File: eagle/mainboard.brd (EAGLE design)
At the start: 100 x 100 mm, 100 parts, among them IC1 74HC02D, IC2 74HC151D, IC3 74HC151D, IC4 74HC590D

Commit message: set board labels and fixed errors
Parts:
- moved C8 1.00 mm to (86.2, -26.8)
- moved R10 0.64 mm to (90.1, 55.0)
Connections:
- net GND: no longer POWER-IN.S1, POWER-IN.S2, POWER-IN.S3, POWER-IN.S4, USB-CONTROLLER1.S1, USB-CONTROLLER1.S2, USB-CONTROLLER1.S3, USB-CONTROLLER1.S4, USB-CONTROLLER2.S1, USB-CONTROLLER2.S2, USB-CONTROLLER2.S3, USB-CONTROLLER2.S4, USB-CONTROLLER3.S1, USB-CONTROLLER3.S2, USB-CONTROLLER3.S3, USB-CONTROLLER3.S4, USB-CONTROLLER4.S1, USB-CONTROLLER4.S2, USB-CONTROLLER4.S3, USB-CONTROLLER4.S4
- net GNDA: no longer CONTROLLER-IN.S1, CONTROLLER-IN.S2, CONTROLLER-IN.S3, CONTROLLER-IN.S4
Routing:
- net VCC: track 15.6 -> 33.7 mm, vias 3 -> 6
- net GND: track 6.55 -> 21.2 mm, vias 3 -> 10
- net N$32: track 3.69 -> 12.6 mm, vias 1 -> 2
- net N$29: track 29.6 -> 36.7 mm
- net GNDA: track 16.7 -> 20.7 mm
- net +3V3: track 100.7 -> 97.5 mm
- net DOWN: track 48.0 -> 45.9 mm
- net VSYNC: track 73.8 -> 75.5 mm
- net N$15: track 27.8 -> 29.4 mm
- net CONTROLLER_CLOCK: track 47.5 -> 48.7 mm
- net VGA_RED: track 73.2 -> 74.4 mm
- net N$27: track 59.9 -> 58.9 mm
- net N$24: track 62.4 -> 61.5 mm
- net N$11: track 37.1 -> 37.9 mm

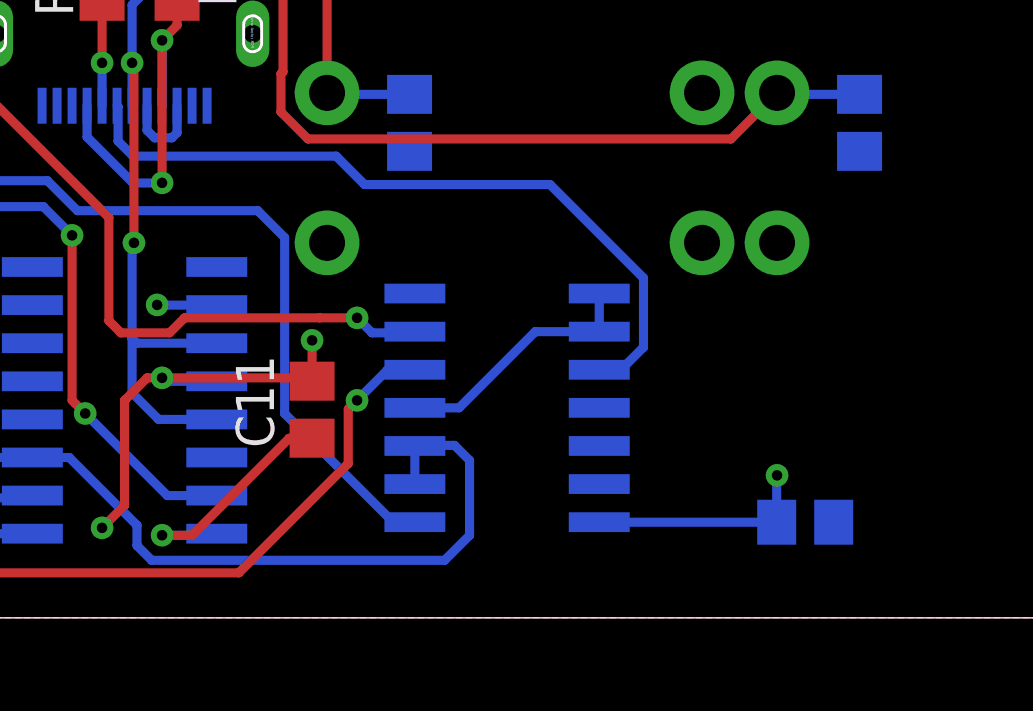
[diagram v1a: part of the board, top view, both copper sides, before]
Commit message: added fancy drawings and logos on the back of the board
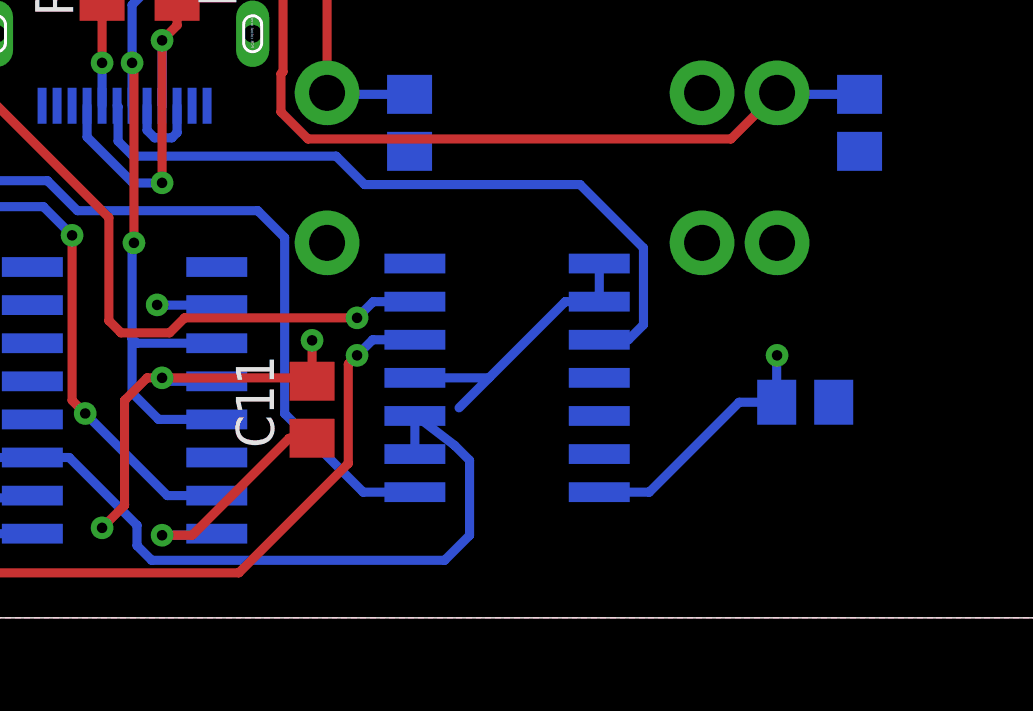
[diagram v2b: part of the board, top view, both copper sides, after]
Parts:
- moved C8 4.00 mm to (86.2, -22.8)
- moved IC1 1.00 mm to (76.2, -22.0)
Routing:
- net N$17: track 8.47 -> 9.88 mm
- net N$11: track 37.9 -> 39.3 mm
- net VCC: track 33.7 -> 35.0 mm
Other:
- board text added: "This board was made by menga-team™ check us out at https://github.com/menga-team/ check the board out at https://github.com/menga-team/MES check the svg 2 polygon converter at https://github.com/menga-team/svg2eagle"

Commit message: some drc improvements
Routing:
- net +3V3: track 97.5 -> 100.7 mm
- net N$17: track 9.88 -> 8.47 mm
- net CONTROLLER_OUT: track 25.1 -> 24.4 mm
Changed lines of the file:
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@@
 <drawing>
 <settings>
-<setting alwaysvectorfont="yes"/>
+<setting alwaysvectorfont="no"/>
 <setting verticaltext="up"/>
 </settings>
-<grid distance="9.84251969" unitdist="mil" unit="mil" style="dots" multiple="1" display="yes" altdistance="0.0625" altunitdist="mm" altunit="mm"/>
+<grid distance="0.25" unitdist="mm" unit="mm" style="dots" multiple="1" display="yes" altdistance="0.03125" altunitdist="mm" altunit="mm"/>
 <layers>
 <layer number="1" name="Top" color="4" fill="1" visible="yes" active="yes"/>
@@
 <param name="mtCopper" value="0.035mm 0.035mm 0.035mm 0.035mm 0.035mm 0.035mm 0.035mm 0.035mm 0.035mm 0.035mm 0.035mm 0.035mm 0.035mm 0.035mm 0.035mm 0.035mm"/>
 <param name="mtIsolate" value="1.5mm 0.15mm 0.2mm 0.15mm 0.2mm 0.15mm 0.2mm 0.15mm 0.2mm 0.15mm 0.2mm 0.15mm 0.2mm 0.15mm 0.2mm"/>
-<param name="mdWireWire" value="6mil"/>
-<param name="mdWirePad" value="6mil"/>
-<param name="mdWireVia" value="6mil"/>
-<param name="mdPadPad" value="6mil"/>
-<param name="mdPadVia" value="6mil"/>
-<param name="mdViaVia" value="6mil"/>
-<param name="mdSmdPad" value="6mil"/>
-<param name="mdSmdVia" value="6mil"/>
-<param name="mdSmdSmd" value="6mil"/>
+<param name="mdWireWire" value="12mil"/>
+<param name="mdWirePad" value="12mil"/>
+<param name="mdWireVia" value="12mil"/>
+<param name="mdPadPad" value="12mil"/>
+<param name="mdPadVia" value="12mil"/>
+<param name="mdViaVia" value="12mil"/>
+<param name="mdSmdPad" value="12mil"/>
+<param name="mdSmdVia" value="12mil"/>
+<param name="mdSmdSmd" value="12mil"/>
 <param name="mdViaViaSameLayer" value="6mil"/>
 <param name="mnLayersViaInSmd" value="2"/>
@@
 </groups>
 <elements>
-<element name="3V3" library="pinhead" library_urn="urn:adsk.eagle:library:325" package="1X01" package3d_urn="urn:adsk.eagle:package:22485/2" value="+3V3" x="84.25" y="63.1875" smashed="yes" rot="R90">
-<attribute name="NAME" x="82.4212" y="61.8413" size="1.27" layer="25" ratio="10" rot="R90"/>
-<attribute name="POPULARITY" value="64" x="185.85" y="140.6575" size="1.778" layer="27" rot="R90" display="off"/>
-<attribute name="VALUE" x="87.425" y="61.9175" size="1.27" layer="27" rot="R90"/>
+<element name="3V3" library="pinhead" library_urn="urn:adsk.eagle:library:325" package="1X01" package3d_urn="urn:adsk.eagle:package:22485/2" value="+3V3" x="84.25" y="63.15625" smashed="yes" rot="R90">
+<attribute name="NAME" x="82.4212" y="61.81005" size="1.27" layer="25" ratio="10" rot="R90"/>
+<attribute name="POPULARITY" value="64" x="185.85" y="140.62625" size="1.778" layer="27" rot="R90" display="off"/>
+<attribute name="VALUE" x="87.425" y="61.88625" size="1.27" layer="27" rot="R90"/>
 </element>
 <element name="5V" library="pinhead" library_urn="urn:adsk.eagle:library:325" package="1X01" package3d_urn="urn:adsk.eagle:package:22485/2" value="+5V" x="94.25" y="8.25" smashed="yes">
@@
 <wire x1="9.75" y1="44.02" x2="9.75" y2="45.5" width="0.3048" layer="16"/>
 <via x="9.75" y="45.5" extent="1-16" drill="0.35"/>
+<wire x1="9.68" y1="54" x2="9.68" y2="55" width="0" layer="19" extent="1-1"/>
+<wire x1="9.68" y1="40.75" x2="9.68" y2="39.75" width="0" layer="19" extent="1-1"/>
+<wire x1="9.68" y1="26.25" x2="9.68" y2="25.25" width="0" layer="19" extent="1-1"/>
+<wire x1="9.68" y1="11.75" x2="9.68" y2="10.75" width="0" layer="19" extent="1-1"/>
 <wire x1="90.07" y1="6.5" x2="90.07" y2="5" width="0" layer="19" extent="1-1"/>
 <wire x1="90.07" y1="8.5" x2="90.07" y2="7.5" width="0" layer="19" extent="1-1"/>
@@
 <wire x1="15.86061875" y1="51.2072" x2="14.8" y2="50.14658125" width="0.3048" layer="1"/>
 <wire x1="14.8" y1="50.14658125" x2="14.8" y2="50" width="0.3048" layer="1"/>
-<wire x1="81.03" y1="63.16" x2="84.25" y2="63.1875" width="0" layer="19" extent="1-1"/>
+<wire x1="84.25" y1="63.15625" x2="81.03375" y2="63.15625" width="0.3048" layer="16"/>
+<wire x1="81.03375" y1="63.15625" x2="81.03" y2="63.16" width="0.3048" layer="16"/>
 <wire x1="37.85" y1="47.92" x2="81.03" y2="63.16" width="0" layer="19" extent="1-1"/>
 <wire x1="20.72" y1="35.41" x2="14.8125" y2="41.95" width="0" layer="19" extent="16-16"/>
@@
 <wire x1="43.75" y1="-20" x2="43.75" y2="-22.45" width="0.3048" layer="16"/>
 <wire x1="43.75" y1="-22.45" x2="43.7" y2="-22.5" width="0.3048" layer="16"/>
-<wire x1="46.9266" y1="-4.075" x2="45.325" y2="-4.075" width="0.3048" layer="16"/>
-<wire x1="45.325" y1="-4.075" x2="44.5" y2="-3.25" width="0.3048" layer="16"/>
-<wire x1="44.5" y1="-3.25" x2="42.75" y2="-3.25" width="0.3048" layer="16"/>
+<wire x1="46.9266" y1="-4.075" x2="44.825" y2="-4.075" width="0.3048" layer="16"/>
+<wire x1="44.825" y1="-4.075" x2="44" y2="-3.25" width="0.3048" layer="16"/>
+<wire x1="44" y1="-3.25" x2="42.75" y2="-3.25" width="0.3048" layer="16"/>
 <wire x1="38.75" y1="-7.25" x2="38.75" y2="-8.75" width="0.3048" layer="16"/>
 <via x="38.75" y="-8.75" extent="1-16" drill="0.35"/>
@@
 <wire x1="68.9875" y1="-24.0125" x2="69.75" y2="-24.0125" width="0.3048" layer="1"/>
 <wire x1="65.7538" y1="-27.2462" x2="68.9875" y2="-24.0125" width="0.3048" layer="1"/>
-<wire x1="46.9266" y1="-2.805" x2="45.548" y2="-2.805" width="0.3048" layer="16"/>
-<wire x1="45.548" y1="-2.805" x2="45.5" y2="-2.853" width="0.3048" layer="16"/>
-<via x="45.5" y="-2.853" extent="1-16" drill="0.35"/>
 <wire x1="79.3234" y1="-25.81" x2="80.99" y2="-25.81" width="0.3048" layer="16"/>
 <wire x1="83.9875" y1="-22.8125" x2="85.2375" y2="-22.8125" width="0.3048" layer="16"/>
 <wire x1="83.9875" y1="-22.8125" x2="80.99" y2="-25.81" width="0.3048" layer="16"/>
+<wire x1="46.9266" y1="-2.805" x2="45.305" y2="-2.805" width="0.3048" layer="16"/>
+<wire x1="45.305" y1="-2.805" x2="45.25" y2="-2.75" width="0.3048" layer="16"/>
+<via x="45.25" y="-2.75" extent="1-16" drill="0.35"/>
 </signal>
 <signal name="CONTROLLER_OUT">
@@
 <wire x1="63.2834" y1="-12.9634" x2="63.25" y2="-12.93" width="0.3048" layer="16"/>
 <wire x1="63.2834" y1="-14.10998125" x2="63.2834" y2="-12.9634" width="0.3048" layer="16"/>
-<wire x1="79.3234" y1="-20.73" x2="80.04618125" y2="-20.73" width="0.3048" layer="16"/>
 <wire x1="78.68338125" y1="-15.5572" x2="71.5" y2="-15.5572" width="0.3048" layer="16"/>
-<wire x1="80.7966" y1="-20.22958125" x2="80.7966" y2="-17.67041875" width="0.3048" layer="16"/>
+<wire x1="80.7966" y1="-17.67041875" x2="80.7966" y2="-20.22958125" width="0.3048" layer="16"/>
 <wire x1="80.7966" y1="-17.67041875" x2="78.68338125" y2="-15.5572" width="0.3048" layer="16"/>
 <wire x1="71.5" y1="-15.5572" x2="70.5524" y2="-14.6096" width="0.3048" layer="16"/>
 <wire x1="70.5524" y1="-14.6096" x2="63.78301875" y2="-14.6096" width="0.3048" layer="16"/>
 <wire x1="63.78301875" y1="-14.6096" x2="63.2834" y2="-14.10998125" width="0.3048" layer="16"/>
-<wire x1="79.3234" y1="-20.73" x2="80.29618125" y2="-20.73" width="0.3048" layer="16"/>
-<wire x1="80.29618125" y1="-20.73" x2="80.7966" y2="-20.22958125" width="0.3048" layer="16"/>
+<wire x1="80.7966" y1="-20.22958125" x2="80.29618125" y2="-20.73" width="0.3048" layer="16"/>
+<wire x1="80.29618125" y1="-20.73" x2="79.3234" y2="-20.73" width="0.3048" layer="16"/>
 </signal>
 <signal name="CONTROLLER_CLOCK">
@@
 <wire x1="49.5" y1="-28.5" x2="67.30908125" y2="-28.5" width="0.3048" layer="1"/>
 <wire x1="67.30908125" y1="-28.5" x2="70.9572" y2="-24.85188125" width="0.3048" layer="1"/>
-<wire x1="73.1766" y1="-20.8234" x2="73.1766" y2="-20.73" width="0.3048" layer="16"/>
 <wire x1="71.25" y1="-21.25" x2="71.77" y2="-20.73" width="0.3048" layer="16"/>
 <wire x1="71.77" y1="-20.73" x2="73.1766" y2="-20.73" width="0.3048" layer="16"/>
@@
 <contactref element="IC3" pad="5"/>
 <contactref element="IC1" pad="6"/>
-<wire x1="73.1766" y1="-19.46" x2="73.1366" y2="-19.5" width="0.3048" layer="16"/>
 <via x="71.25" y="-20" extent="1-16" drill="0.35"/>
 <via x="55" y="-7.75" extent="1-16" drill="0.35"/>
@@
 <contactref element="IC1" pad="8"/>
 <contactref element="IC1" pad="9"/>
-<wire x1="73.1766" y1="-22" x2="75.649384375" y2="-22" width="0.3048" layer="16"/>
-<wire x1="78.18938125" y1="-19.46" x2="74.649384375" y2="-23" width="0.3048" layer="16"/>
-<wire x1="78.18938125" y1="-19.46" x2="79.3234" y2="-19.46" width="0.3048" layer="16"/>
+<wire x1="75.649384375" y1="-22" x2="73.1766" y2="-22" width="0.3048" layer="16"/>
 <wire x1="79.3234" y1="-19.46" x2="79.3234" y2="-18.19" width="0.3048" layer="16"/>
-<wire x1="74.649384375" y1="-23" x2="75.649384375" y2="-22" width="0" layer="19" extent="16-16"/>
+<wire x1="79.3234" y1="-19.46" x2="78.189384375" y2="-19.46" width="0.3048" layer="16"/>
+<wire x1="78.189384375" y1="-19.46" x2="75.649384375" y2="-22" width="0.3048" layer="16"/>
 </signal>
 <signal name="N$32">
@@
 <mfgpreviewcolor name="substratecolor" color="0xFF786E46"/>
 </mfgpreviewcolors>
+<errors>
+</errors>
 </board>
 </drawing>

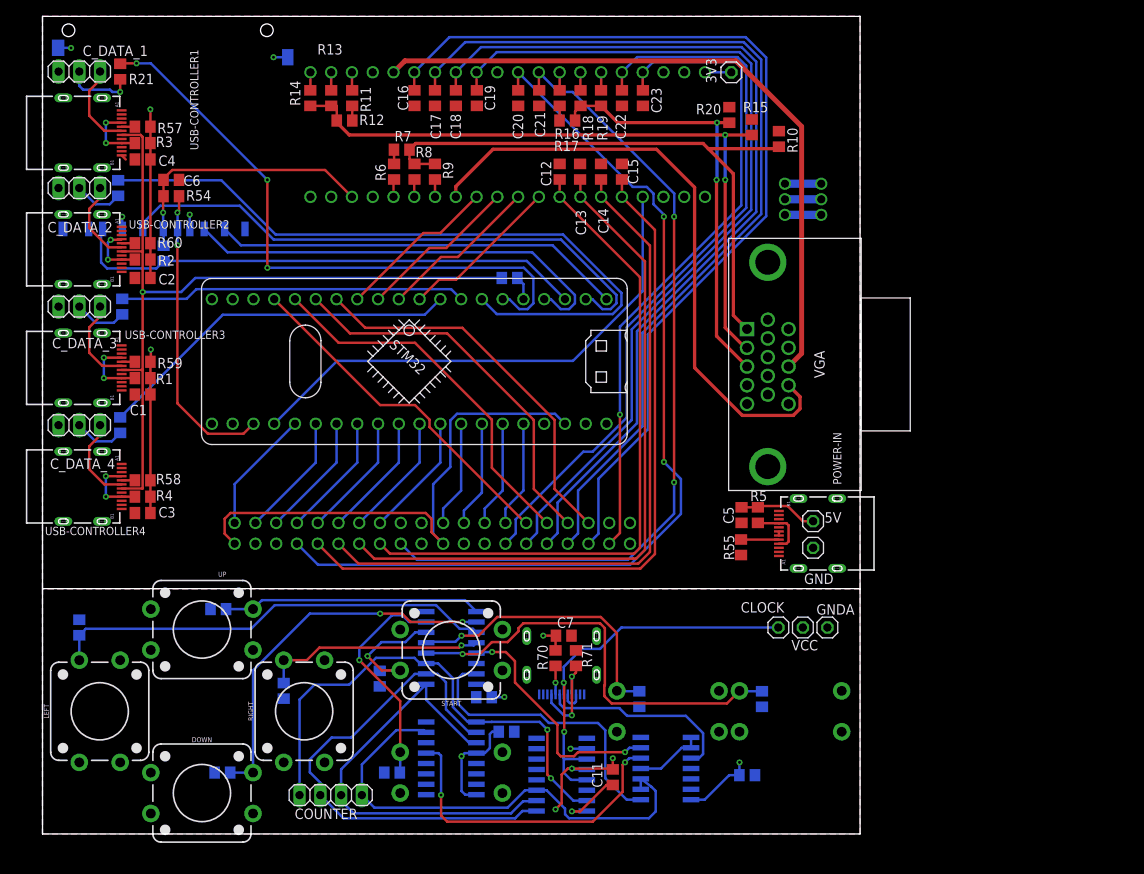
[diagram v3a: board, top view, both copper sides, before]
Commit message: fixed errors, rewired controller clock and fixed buttons on wrong layer
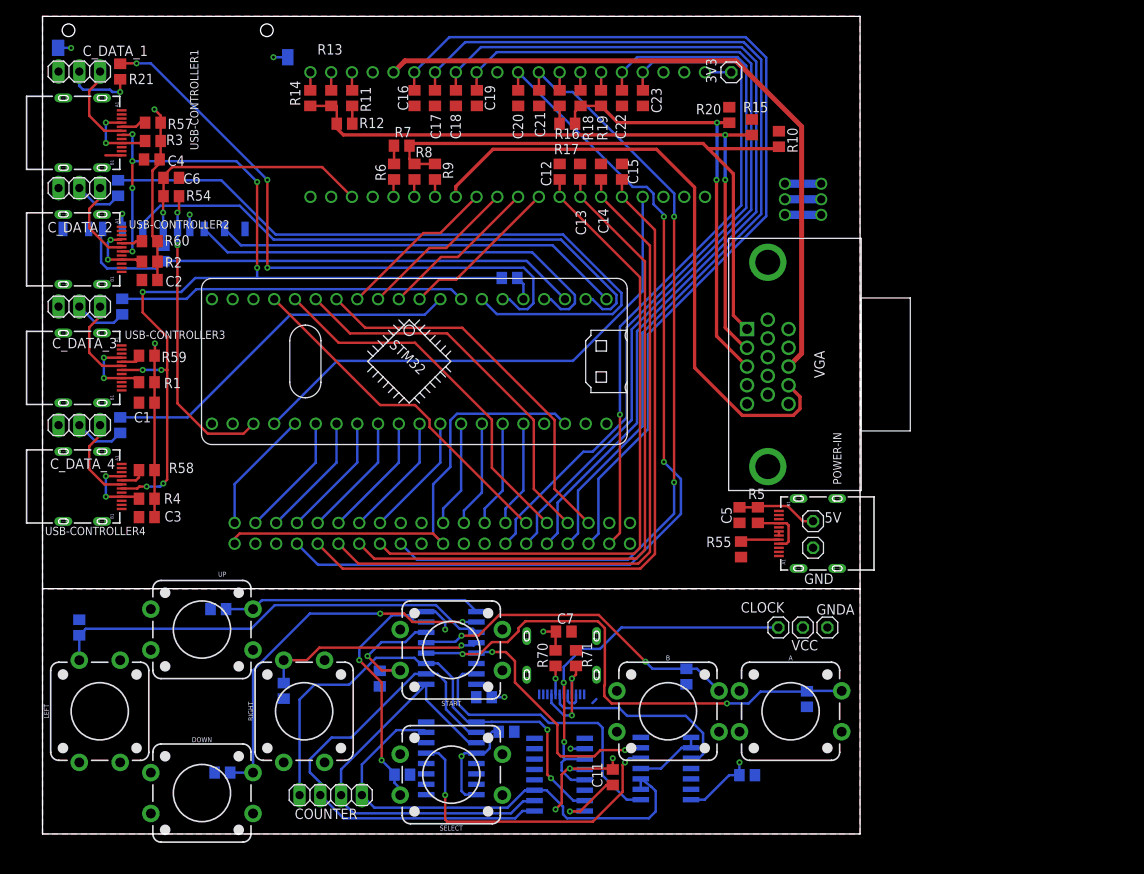
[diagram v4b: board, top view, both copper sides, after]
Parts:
- moved R63 6.37 mm to (78.8, -10.8)
- moved R64 5.50 mm to (93.5, -13.5)
- moved R57 1.35 mm to (13.5, 57.0)
- moved R58 1.35 mm to (12.8, 14.5)
- moved R3 1.27 mm to (13.5, 54.8)
- moved R61 1.27 mm to (44.0, -22.8), turned to 180 degrees
- moved C4 1.12 mm to (13.4, 52.5)
- moved C1 1.12 mm to (12.8, 22.8)
- moved R59 0.90 mm to (12.8, 28.5)
- moved C2 0.90 mm to (13.1, 37.8)
- moved R2 0.90 mm to (13.1, 40.0)
- moved R60 0.90 mm to (13.1, 42.5)
- moved C3 0.71 mm to (12.8, 8.75)
- moved R1 0.71 mm to (12.8, 25.2)
- moved R4 0.56 mm to (12.8, 11.0)
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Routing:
- net C_CLOCK: track 98.0 -> 125.5 mm, vias 1 -> 11
- net A: track 52.6 -> 62.5 mm, vias 1 -> 2
- net B: track 35.3 -> 41.1 mm, vias 1 -> 2
- net +3V3: track 100.7 -> 95.0 mm
- net SELECT: track 27.5 -> 30.2 mm, vias 1 -> 2
- net +5V: track 50.3 -> 53.0 mm
- net VCC: track 35.2 -> 37.3 mm
- net GND: track 21.2 -> 22.8 mm
- net N$13: track 1.62 -> 3.15 mm
- net N$6: track 1.62 -> 3.08 mm
- net N$5: track 7.98 -> 9.33 mm
- net GNDA: track 20.7 -> 21.9 mm
- net N$14: track 1.62 -> 2.65 mm
- net N$31: track 1.62 -> 2.58 mm
- net N$2: track 7.24 -> 8.20 mm
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
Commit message: huber approve check has been given
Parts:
- moved C5 8.25 mm to (77.0, 9.00)
- moved R5 5.50 mm to (82.0, 9.00)
- moved R66 5.50 mm to (10.0, -4.75)
- moved GNDA 4.00 mm to (92.0, -4.75)
- moved VCC 3.75 mm to (89.2, -4.75)
- moved CLOCK 3.50 mm to (86.5, -4.75)
- moved R55 0.56 mm to (85.9, 5.06)
- moved R10 0.25 mm to (90.1, 54.8)
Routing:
- net +5V: track 53.0 -> 61.2 mm
- net N$1: track 7.16 -> 12.7 mm
- net HSYNC: track 83.8 -> 89.1 mm
- net CONTROLLER_CLOCK: track 48.4 -> 44.9 mm
- net VSYNC: track 75.5 -> 78.2 mm
- net LEFT: track 54.5 -> 52.7 mm
- net N$8: track 4.73 -> 4.14 mm
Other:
- board size 100 x 100 mm -> 100.2 x 100 mm
